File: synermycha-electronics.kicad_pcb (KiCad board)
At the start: 4 copper layers, 50 x 75 mm, 178 parts, among them IC1 CYPD3177, J12 Conn_01x05, J13 Conn_01x05, J14 Conn_01x05, J15 Conn_01x05, J16 Conn_01x05, J17 CK-JS102011SAQN, J2 Conn_01x02, J3 Conn_01x02, J4 USB_C_Receptacle_USB2.0, J6 A1250WV-S-4P, J7 Conn_01x04, J8 Conn_01x04, Q1 IRLML9301TRPBF, Q2 IRLML9301TRPBF, Q3 IRLML9301TRPBF, Q4 BC847, Q5 BC856, Q7 IRLML9301TRPBF, SW1 DTSM32N, SW2 DTSM32N, SW3 DTSM32N, SW4 DTSM32N, U1 LM1117LDX, U12 MPU-9250, U13 STM32F446RETx, U14 STM14_SW, U2 LDFM33PVR, U3 RN4871U-V_RM118, U4 DRV8835, U5 MCP73213, U6 ETA3000, Y1 16Mhz, 18pF

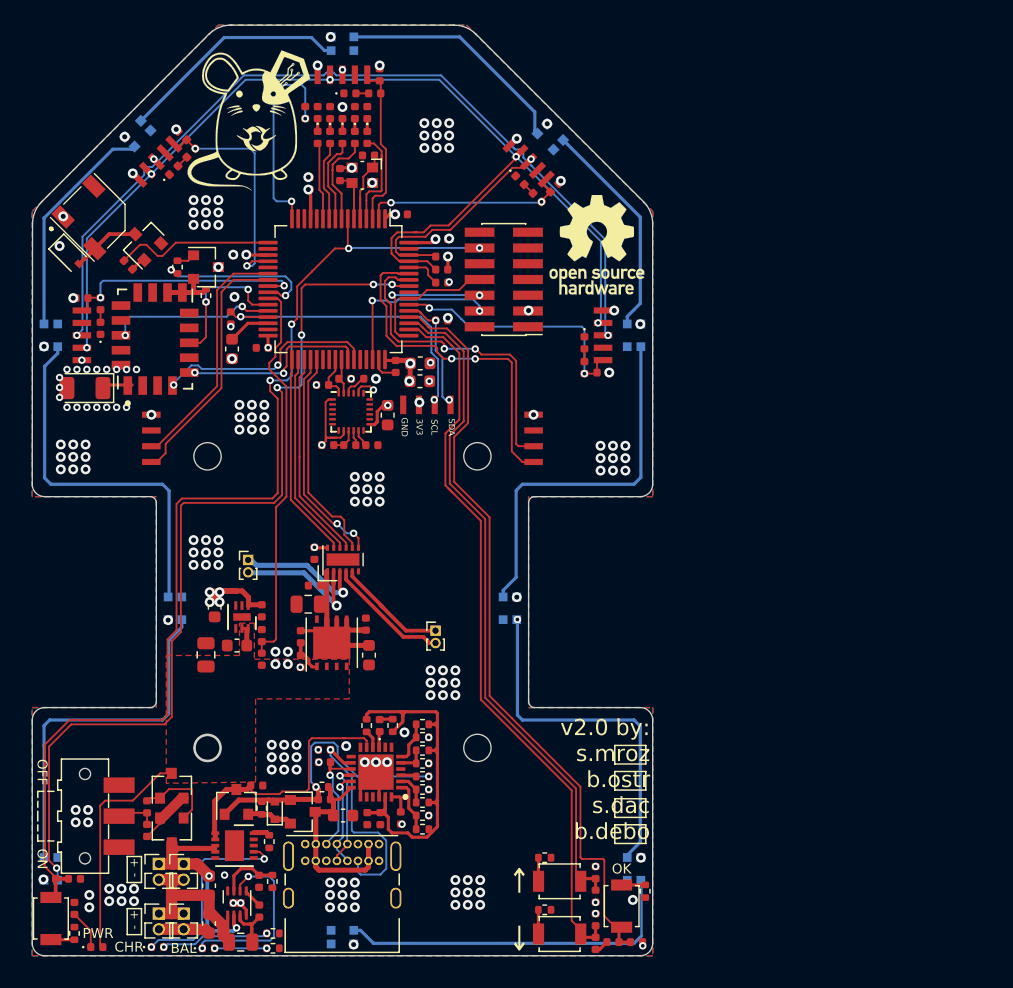
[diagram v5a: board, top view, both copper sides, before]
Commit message: Zmieniono kontroler USB-PD
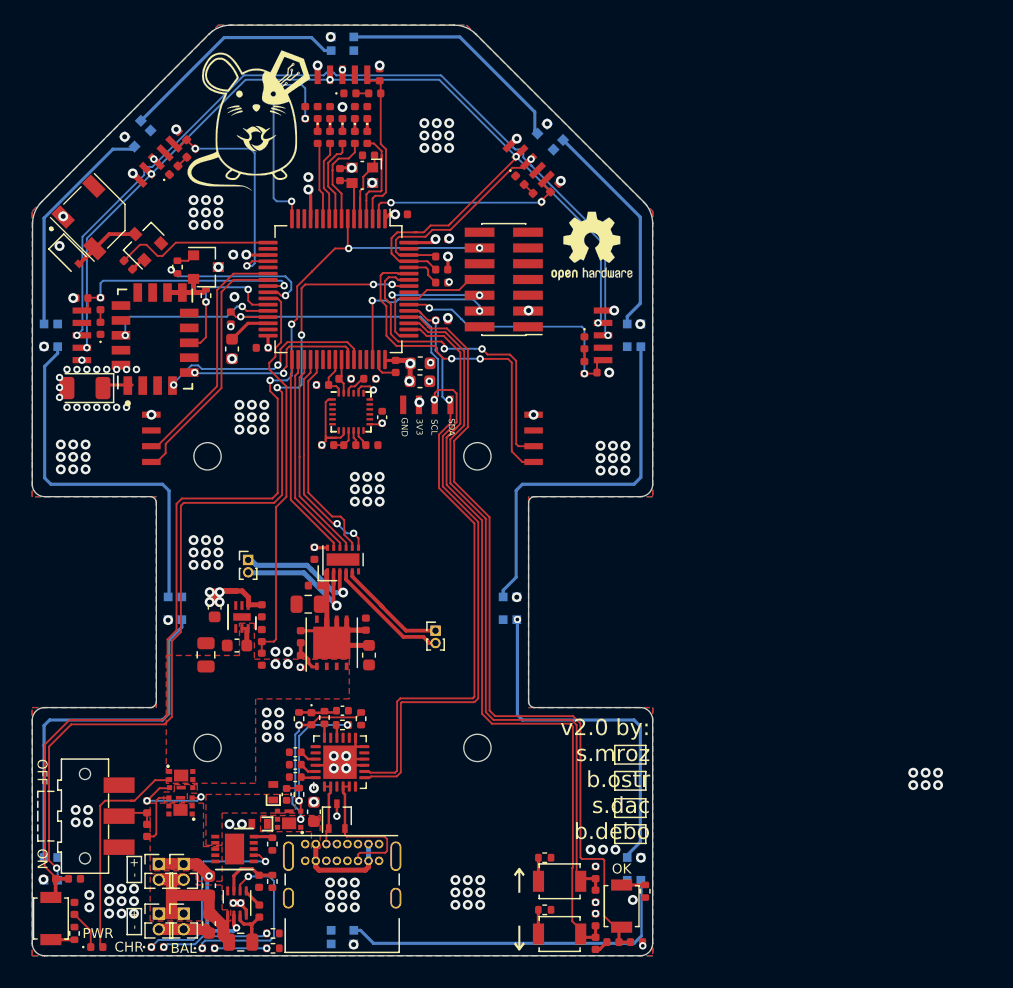
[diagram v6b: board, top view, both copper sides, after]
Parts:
- removed C18: 0.1uF, Capacitor_SMD:C_0402_1005Metric
- removed C19: 1uF, Capacitor_SMD:C_0402_1005Metric
- removed IC1: CYPD3177, CYPD3177-24LQXI:QFN50P400X400X60-25N-D
- removed Q7: IRLML9301TRPBF, Package_TO_SOT_SMD:SOT-23
- removed R34, R41: 5K1, Resistor_SMD:R_0402_1005Metric
- removed R35: 1K, Resistor_SMD:R_0402_1005Metric
- removed R44: 2K4, Resistor_SMD:R_0402_1005Metric
- removed R45: DNP, Resistor_SMD:R_0402_1005Metric
- removed R47: 0, Resistor_SMD:R_0402_1005Metric
- removed R48: 10K, Resistor_SMD:R_0402_1005Metric
- removed R53: 2k, Resistor_SMD:R_0402_1005Metric
- removed the REF** at (36.9, 168.5)
- removed the REF** at (57.5, 140.7)
- added D28: ESDA25W, Package_TO_SOT_SMD:SOT-323_SC-70, F.Cu at (36.5, 186.8)
- added D29: ESDA25P35, footprints:1610, F.Cu at (31.4, 184.8)
- added REF**: OSHW-Logo2_7.3x6mm_SilkScreen, Symbol:OSHW-Logo2_7.3x6mm_SilkScreen, F.Cu at (57.1, 140.8)
- added U7: STUSB4500QTR, Package_DFN_QFN:QFN-24-1EP_4x4mm_P0.5mm_EP2.7x2.7mm, F.Cu at (36.8, 182.4)
- C14: value 390pF -> 1uF
- C17: value 1uF -> 0.1uF
- C26: value 10uF -> 0.1uF; footprint Capacitor_SMD:C_0603_1608Metric -> Capacitor_SMD:C_0402_1005Metric
- C5: value 390pF -> 4.7uF; footprint Capacitor_SMD:C_0402_1005Metric -> Capacitor_SMD:C_0603_1608Metric
- C8: value 10uF -> 1uF; footprint Capacitor_SMD:C_0603_1608Metric -> Capacitor_SMD:C_0402_1005Metric
- D24: value 9V -> ESDA25P35; footprint Diode_SMD:D_SOD-523 -> footprints:1610
- D25: value RED -> CDBQR0130L-HF; footprint LED_SMD:LED_0402_1005Metric -> Diode_SMD:D_0402_1005Metric
- Q1, Q2, Q3: value IRLML9301TRPBF -> SSM6J507NU; footprint Package_TO_SOT_SMD:SOT-23 -> footprints:UDFN6B
- R16: value 1K -> 470
- R18: value 5K1 -> 100K
- R21: value 1K -> 18K
- R28: value 47K -> 100K
- moved R18 10.2 mm to (38.5, 178.9), turned to 270 degrees
- moved R21 9.74 mm to (37.0, 179.4), turned to 180 degrees
- moved C16 9.53 mm to (33.2, 182.6), turned to 180 degrees
- moved R17 9.22 mm to (35.5, 178.8), turned to 90 degrees
- moved C8 8.45 mm to (37.0, 178.2)
- moved C17 7.80 mm to (32.5, 185.0), turned to 90 degrees
- moved R16 5.80 mm to (33.5, 178.9), turned to 90 degrees
- moved D25 5.53 mm to (34.5, 178.9), turned to 270 degrees
- moved Q3 4.80 mm to (24.0, 183.8), turned to 0 degrees
- moved C15 4.47 mm to (33.2, 181.6)
- moved C5 4.09 mm to (34.7, 186.4), turned to 90 degrees
- moved C14 3.22 mm to (33.2, 183.6)
- moved R28 3.20 mm to (33.5, 185.0), turned to 270 degrees
- moved Q1 2.10 mm to (23.9, 185.9), turned to 180 degrees
- moved D24 1.67 mm to (30.3, 187.4), turned to 180 degrees
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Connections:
- C15 pad 2: Net-(C15-Pad2) -> GND
- C17 pad 1: /Power Section/CYPD_+3V3 -> /Power Section/VDRIVE
- C17 pad 2: GND -> Net-(C17-Pad2)
- C5 pad 1: Net-(C5-Pad1) -> /Power Section/VBUS
- C8 pad 1: Net-(C15-Pad1) -> Net-(C8-Pad1)
- D24 pad 1: Net-(D24-Pad1) -> /Power Section/VBUS
- D24 pad 2: Net-(C15-Pad2) -> GND
- D25 pad 1: Net-(D25-Pad1) -> Net-(C8-Pad1)
- D25 pad 2: Net-(D25-Pad2) -> /Power Section/VBUS
- J4 pad A4: Net-(C15-Pad1) -> /Power Section/VBUS
- J4 pad A5: Net-(C5-Pad1) -> Net-(D28-Pad1)
- J4 pad A6: /Power Section/D+ -> Net-(J4-PadA6)
- J4 pad A7: /Power Section/D- -> Net-(J4-PadA7)
- J4 pad A9: Net-(C15-Pad1) -> /Power Section/VBUS
- J4 pad B4: Net-(C15-Pad1) -> /Power Section/VBUS
- J4 pad B5: Net-(C14-Pad1) -> Net-(D28-Pad2)
- J4 pad B6: /Power Section/D+ -> Net-(J4-PadB6)
- J4 pad B7: /Power Section/D- -> Net-(J4-PadB7)
- J4 pad B9: Net-(C15-Pad1) -> /Power Section/VBUS
- Q1 pad 1: Net-(Q1-Pad1) -> /Power Section/BATT+
- Q1 pad 2: Net-(Q1-Pad2) -> /Power Section/BATT+
- Q1 pad 3: /Power Section/BATT+ -> Net-(Q1-Pad3)
- Q2 pad 1: Net-(C15-Pad2) -> /Power Section/VBUS
- Q2 pad 2: Net-(D24-Pad1) -> /Power Section/VBUS
- Q2 pad 3: Net-(C15-Pad1) -> Net-(Q2-Pad3)
- Q3 pad 1: Net-(C15-Pad2) -> /Power Section/VCC
- Q3 pad 2: Net-(D24-Pad1) -> /Power Section/VCC
- Q3 pad 3: Net-(C19-Pad1) -> Net-(Q1-Pad3)
- R16 pad 1: Net-(C15-Pad1) -> /Power Section/VBUS
- R16 pad 2: Net-(C15-Pad2) -> Net-(C8-Pad1)
- R17 pad 1: Net-(C15-Pad2) -> Net-(R17-Pad1)
- R17 pad 2: Net-(IC1-Pad3) -> Net-(C8-Pad1)
- R18 pad 1: /Power Section/CYPD_+3V3 -> /Power Section/VBUS
- R18 pad 2: Net-(IC1-Pad1) -> Net-(Q2-Pad3)
- R21 pad 1: Net-(IC1-Pad1) -> Net-(Q2-Pad3)
- R21 pad 2: GND -> Net-(R21-Pad2)
- R28 pad 1: Net-(D24-Pad1) -> Net-(C17-Pad2)
- R28 pad 2: Net-(C15-Pad2) -> Net-(Q2-Pad3)
- R51 pad 2: Net-(Q1-Pad2) -> Net-(Q1-Pad4)
- R52 pad 2: Net-(Q1-Pad1) -> Net-(Q1-Pad3)
- U5 pad 1: Net-(C19-Pad1) -> /Power Section/VDRIVE
- U5 pad 2: Net-(C19-Pad1) -> /Power Section/VDRIVE
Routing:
- net /LED & Oled & Buzzer/LCD_SCL: track 25.2 -> 70.7 mm
- net /LED & Oled & Buzzer/LCD_SDA: track 10.5 -> 50.3 mm
- net /Power Section/CYPD_+3V3: track 34.6 -> 0.00 mm
- net Net-(C15-Pad2): track 24.0 -> 0.00 mm, vias 2 -> 0
- net /Power Section/VBUS: track 0.00 -> 21.7 mm, vias 0 -> 2
- net Net-(C19-Pad1): track 21.2 -> 0.00 mm
- net Net-(C14-Pad1): track 20.2 -> 1.18 mm, vias 1 -> 0
- net Net-(C15-Pad1): track 17.5 -> 1.39 mm
- net Net-(D28-Pad2): track 0.00 -> 11.9 mm
- net /Power Section/BATT+: track 22.9 -> 12.4 mm
- net Net-(Q2-Pad3): track 0.00 -> 10.5 mm, vias 0 -> 2
- net Net-(C5-Pad1): track 10.3 -> 0.00 mm, vias 1 -> 0
- net /Power Section/D-: track 8.37 -> 0.00 mm, vias 1 -> 0
- net /Power Section/D+: track 7.72 -> 0.00 mm, vias 1 -> 0
- net Net-(Q1-Pad3): track 0.00 -> 7.43 mm, vias 0 -> 2
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- added copper zone on F.Cu, net /Power Section/BATT+
- added copper zone on F.Cu, net /Power Section/BATT_M
- added copper zone on F.Cu, net /Power Section/VBUS
- added copper zone on F.Cu, net /Power Section/VDRIVE
- added copper zone on F.Cu, net Net-(Q1-Pad4)

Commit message: Myszka może być wyłączona także podczas zasilania z USB. Zmiany na PCB
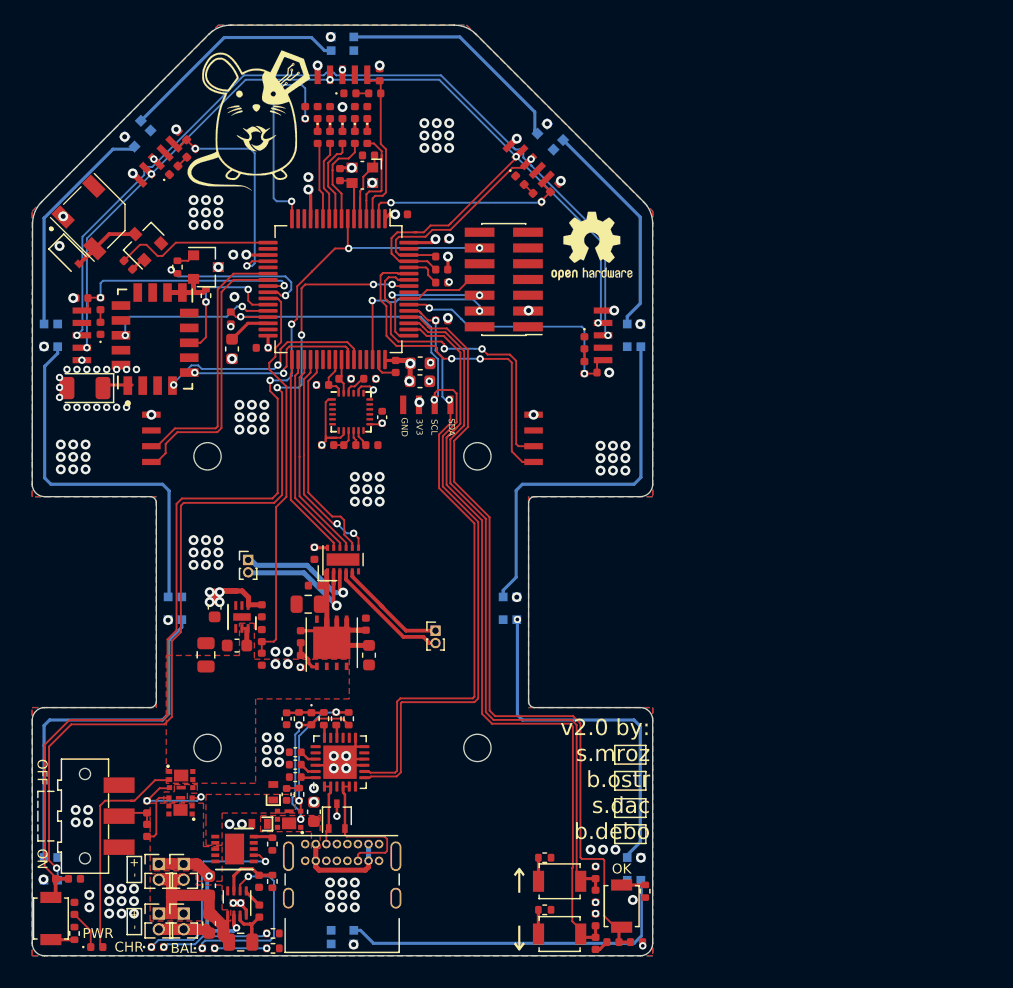
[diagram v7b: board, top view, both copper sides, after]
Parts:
- moved C8 4.55 mm to (32.5, 178.9), turned to 270 degrees
- moved G*** 1.00 mm to (37.0, 141.0)
- moved R18 1.00 mm to (37.5, 178.9), turned to 90 degrees
- moved R21 0.71 mm to (36.5, 178.9), turned to 270 degrees
- moved R17 0.11 mm to (35.5, 178.9)
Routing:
- net /Encoders/ENC_L_B: track 19.7 -> 21.6 mm
- net /Encoders/ENC_L_A: track 20.5 -> 22.3 mm
- net GND: vias 159 -> 144
- removed copper zone on In2.Cu, net GND

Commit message: Kosmetyka
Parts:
- added D30: 30V,2A, Diode_SMD:D_SOD-123F, F.Cu at (27.4, 184.8)
- added Q6: SSM6J507NU, footprints:UDFN6B, F.Cu at (24.0, 186.1)
- added R34: 100K, Resistor_SMD:R_0402_1005Metric, F.Cu at (22.0, 186.0)
- C26: value 0.1uF -> 10uF
- moved Q1 2.58 mm to (24.0, 188.5)
- moved R51 0.47 mm to (21.5, 187.5), turned to 0 degrees
- moved R52 0.25 mm to (21.0, 186.0)
- moved Q3 0.10 mm to (24.0, 183.7)
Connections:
- Q3 pad 4: Net-(Q1-Pad4) -> Net-(D30-Pad1)
- Q3 pad S: Net-(Q1-Pad4) -> Net-(D30-Pad1)
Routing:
- net /Power Section/VDRIVE: track 0.00 -> 6.42 mm, vias 0 -> 2
- net Net-(Q1-Pad4): track 4.63 -> 1.22 mm
- net /Power Section/VCC: track 19.8 -> 22.2 mm
- net Net-(Q1-Pad3): track 7.43 -> 9.74 mm
- net Net-(J17-Pad2): track 3.29 -> 4.30 mm
- added copper zone on F.Cu, net Net-(D30-Pad1)
